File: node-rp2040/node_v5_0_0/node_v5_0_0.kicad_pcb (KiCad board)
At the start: 4 copper layers, 45.7 x 76.2 mm, 107 parts, among them J1 Conn_01x02_Pin, J10 Connector, USB-TYPE-C-16P, J2 U.FL, J3 Conn_Coaxial, J4 Conn_02x08_Odd_Even, J5 Conn_02x02_Odd_Even, J6 U.FL, J7 Conn_01x02_Pin, J8 Conn_01x02_Pin, J9 U.FL, Q1 DMG2301L, SW1 PTS636 SM50J SMTR LFS, SW2 PTS636 SM50J SMTR LFS, SW3 PTS636 SM50J SMTR LFS, U1 RP2040, U11 1042240820, U12 CAT24M01W, U14 W25Q128, U2 USBLC6-2SC6, U3 AP2112K-3.3, U4 CAT3200-5, U5 MCP73831-2-OT, U6 RFM69HCW, U7 PCF8523T, U8 SP3485EN, U9 SIM7080G

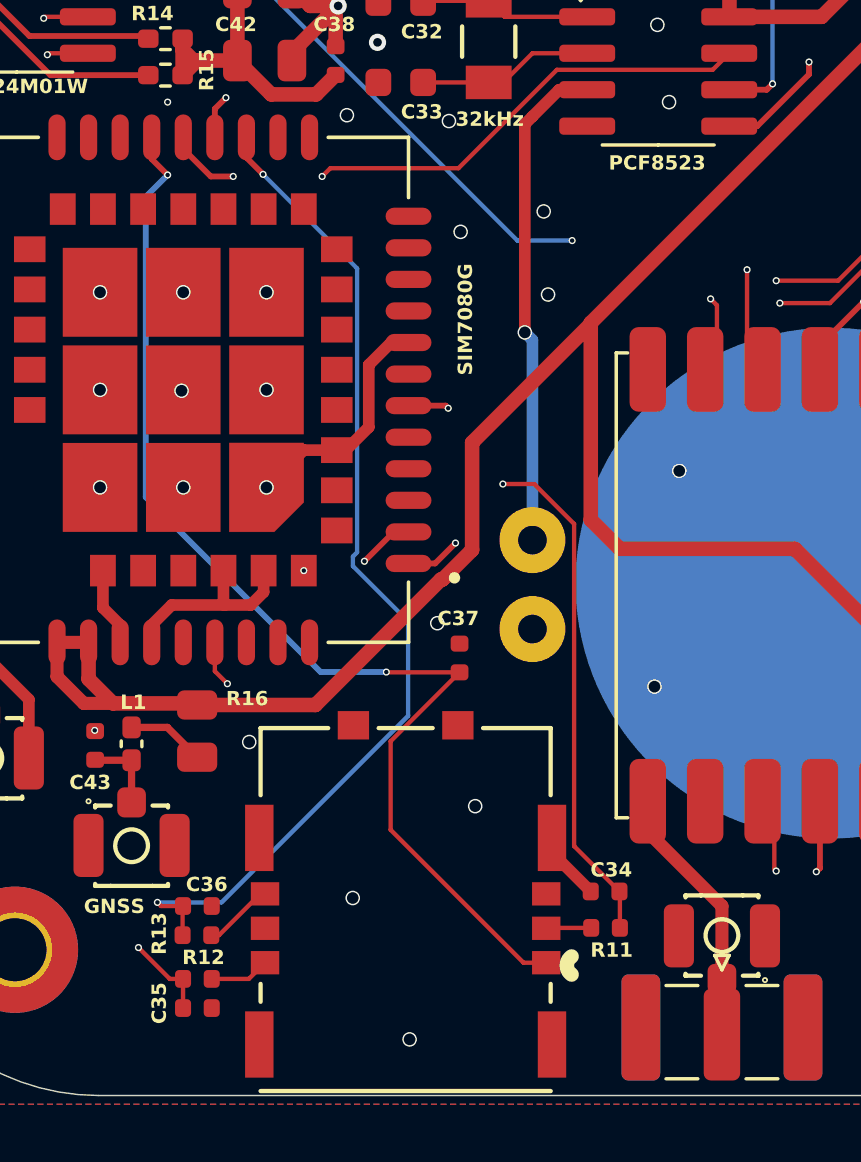
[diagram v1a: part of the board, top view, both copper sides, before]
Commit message: i should have made this more than one commit but: 1) started poking around in v5 to find and solve a sim card problem, forgot about it and moved on 2) created v6, modified the schematic somewhat, removed some parts, began laying out the pcb again this time as a 6 layer board 3) fixed the library setup so now it uses symbols and footprints from the packages available alongside kicad (in void linux at least) for all standard stuff PLUS the wisdom libraries and the jlcpcb prefered parts library
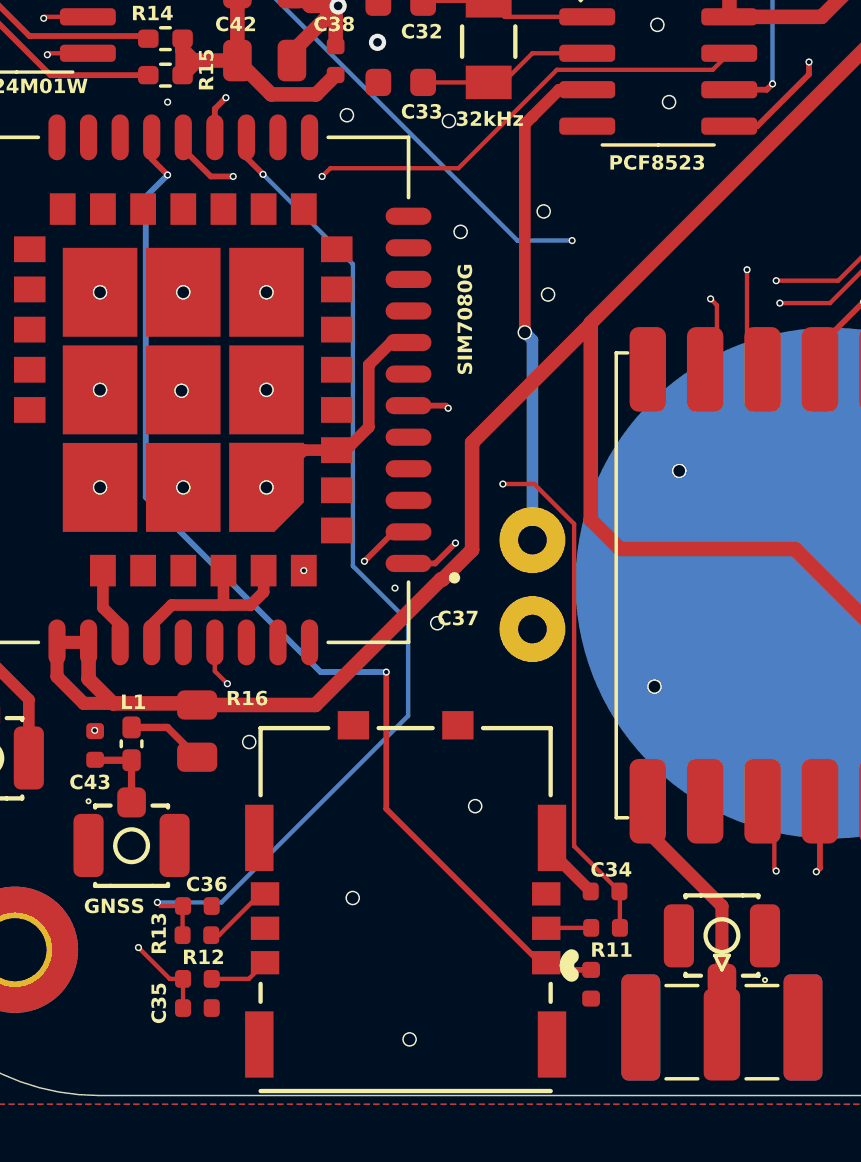
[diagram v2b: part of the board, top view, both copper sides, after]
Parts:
- moved C37 12.3 mm to (51.3, 98.3), turned to -90 degrees
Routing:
- net /PERIPHERALS/SIM_CLK: track 76.7 -> 40.6 mm, vias 2 -> 3
- net /PERIPHERALS/SIM_VCC: track 40.4 -> 38.2 mm
